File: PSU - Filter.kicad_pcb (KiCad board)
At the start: 2 copper layers, 111.8 x 63.5 mm, 36 parts, among them J2 +12V, J3 GND, J4 -12V, J5 +12 GND -12, U1 LM317, U2 LM337

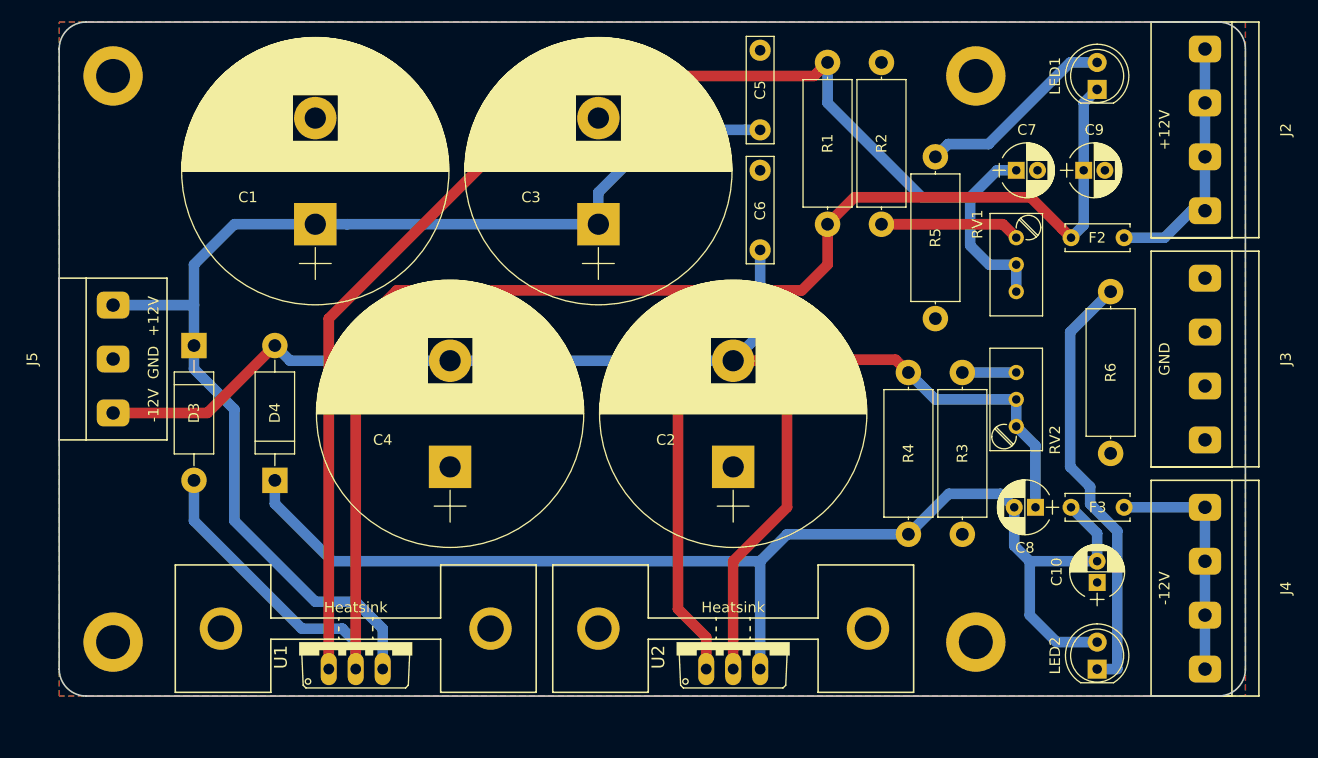
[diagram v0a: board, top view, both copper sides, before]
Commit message: Release client. Fixed a short in +12 branch Changed 10uF footprint to 6.3/2.5mm New KiCad standard library Pointers to the KraakenStuffLib library
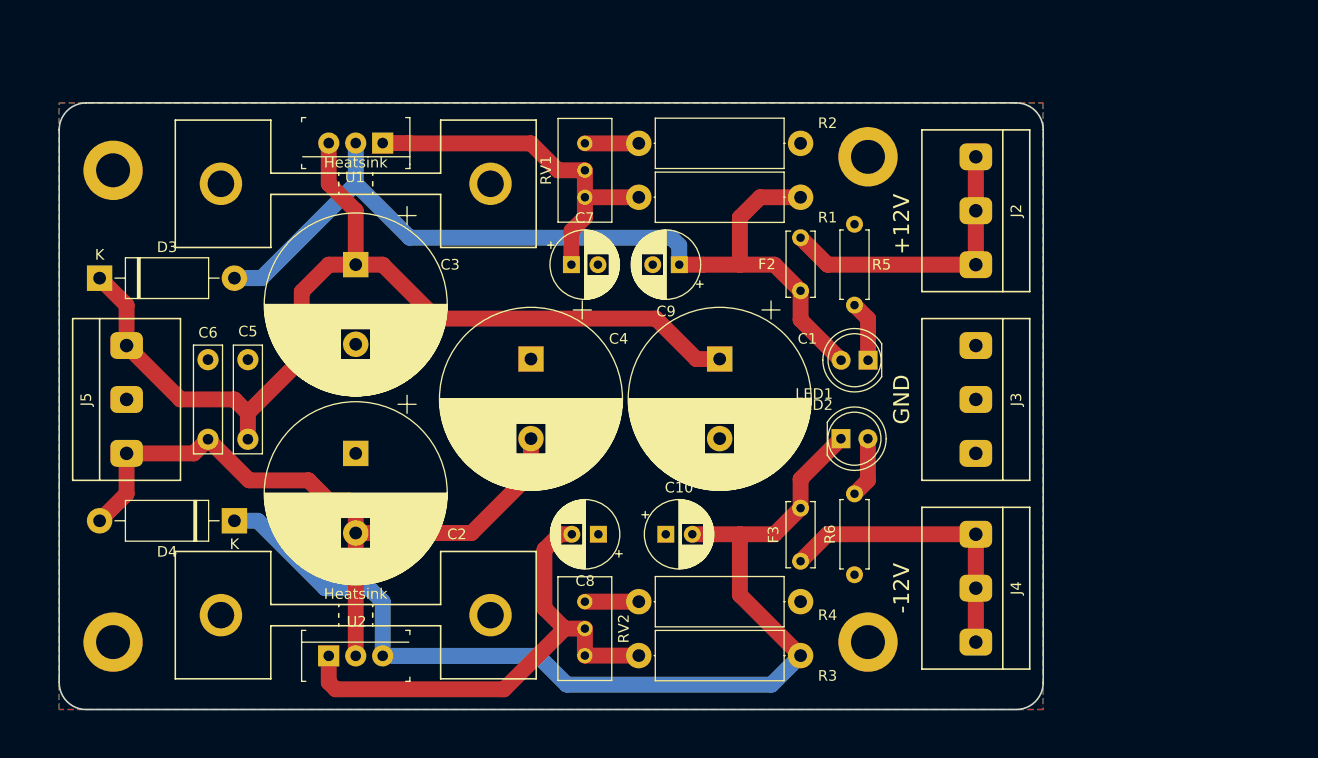
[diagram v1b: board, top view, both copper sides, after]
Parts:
- C1, C2, C3, C4: footprint Capacitors_THT:CP_Radial_D25.0mm_P10.00mm_SnapIn -> Capacitor_THT:CP_Radial_D17.0mm_P7.50mm
- C10, C7, C9: footprint Capacitors_THT:CP_Radial_D5.0mm_P2.00mm -> Capacitor_THT:CP_Radial_D6.3mm_P2.50mm
- C5, C6: footprint Capacitors_THT:C_Rect_L10.0mm_W2.5mm_P7.50mm_MKS4 -> Capacitor_THT:C_Rect_L10.0mm_W2.5mm_P7.50mm_MKS4
- C8: value 4.7u -> 10u; footprint Capacitors_THT:CP_Radial_D5.0mm_P2.00mm -> Capacitor_THT:CP_Radial_D6.3mm_P2.50mm
- D3, D4: footprint Diodes_THT:D_DO-15_P12.70mm_Horizontal -> Diode_THT:D_DO-15_P12.70mm_Horizontal
- F2, F3: footprint Capacitors_THT:C_Disc_D6.0mm_W2.5mm_P5.00mm -> Capacitor_THT:C_Disc_D6.0mm_W2.5mm_P5.00mm
- J2, J3, J4: footprint MojaBiblioteka:Klema x4 -> KraakenStuff:Klema x3
- J5: value +12 GND -12 -> PWR_IN; footprint MojaBiblioteka:Klema x3 -> KraakenStuff:Klema x3
- LED1, LED2: footprint LEDs:LED_D5.0mm -> LED_THT:LED_D5.0mm
- R1, R2, R3, R4: footprint Resistors_THT:R_Axial_DIN0414_L11.9mm_D4.5mm_P15.24mm_Horizontal -> Resistor_THT:R_Axial_DIN0414_L11.9mm_D4.5mm_P15.24mm_Horizontal
- R5, R6: footprint Resistors_THT:R_Axial_DIN0414_L11.9mm_D4.5mm_P15.24mm_Horizontal -> Resistor_THT:R_Axial_DIN0207_L6.3mm_D2.5mm_P7.62mm_Horizontal
- RV1, RV2: footprint Potentiometers:Potentiometer_Trimmer_Bourns_3296W -> Potentiometer_THT:Potentiometer_Bourns_3296W_Vertical
- U1, U2: footprint MusicThingModular:TO220V -> KraakenStuff:TO-220-3
- moved C5 56.4 mm to (81.3, 90.1)
- moved C6 55.0 mm to (77.5, 82.6)
- moved Heatsink 55.0 mm to (91.4, 66.0)
- moved U1 47.1 mm to (94.0, 62.2), turned to 180 degrees
- moved RV2 46.0 mm to (113.0, 110.5)
- moved C7 42.8 mm to (111.8, 73.7)
- moved RV1 41.6 mm to (113.0, 62.2)
- moved C8 41.3 mm to (114.3, 99.1)
- moved C10 40.9 mm to (120.7, 99.1), turned to 0 degrees
- moved C1 40.2 mm to (125.7, 82.5), turned to 270 degrees
- moved C9 39.1 mm to (121.9, 73.7), turned to 180 degrees
- moved U2 38.1 mm to (88.9, 110.5)
- moved R4 36.8 mm to (118.1, 110.5), turned to 0 degrees
- moved C2 35.6 mm to (91.4, 91.4), turned to 270 degrees
- moved LED1 33.4 mm to (139.7, 82.7), turned to 180 degrees
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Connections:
- C8 pad 1: Net-(C8-Pad1) -> GND
- C8 pad 2: Net-(C10-Pad2) -> Net-(C8-Pad2)
- LED1 pad 1: Net-(C9-Pad1) -> Net-(LED1-Pad1)
- LED1 pad 2: Net-(LED1-Pad2) -> Net-(C9-Pad1)
- LED2 pad 1: Net-(LED2-Pad1) -> Net-(C10-Pad2)
- LED2 pad 2: Net-(C10-Pad2) -> Net-(LED2-Pad2)
- R4 pad 1: Net-(C8-Pad1) -> Net-(C8-Pad2)
- R5 pad 1: Net-(LED1-Pad2) -> Net-(LED1-Pad1)
- R6 pad 2: Net-(LED2-Pad1) -> Net-(LED2-Pad2)
- RV2 pad 1: Net-(C8-Pad1) -> Net-(C8-Pad2)
- RV2 pad 2: Net-(C8-Pad1) -> Net-(C8-Pad2)
- U2 pad 1: Net-(C8-Pad1) -> Net-(C8-Pad2)
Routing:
- net Net-(C7-Pad1): track 128.5 -> 34.6 mm
- net Net-(C8-Pad1): track 79.4 -> 0.00 mm
- net Net-(C9-Pad1): track 149.6 -> 85.2 mm
- net Net-(C8-Pad2): track 0.00 -> 48.3 mm
- net Net-(LED2-Pad1): track 40.9 -> 0.00 mm
- net -12_IN: track 108.1 -> 68.3 mm, vias 1 -> 0
- net +12_IN: track 115.7 -> 94.1 mm
- net Net-(C10-Pad2): track 118.0 -> 97.0 mm
- net Net-(LED1-Pad2): track 18.9 -> 0.00 mm
- net Net-(R2-Pad1): track 13.2 -> 5.08 mm
- net Net-(LED1-Pad1): track 0.00 -> 5.72 mm
- net Net-(LED2-Pad2): track 0.00 -> 5.72 mm
- net Net-(F3-Pad1): track 22.9 -> 27.7 mm
- net Net-(F2-Pad1): track 23.9 -> 27.7 mm
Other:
- board size 111.8 x 63.5 mm -> 92.7 x 57.2 mm
- net class Default: trace_width 1 -> 1.5
- board text removed: "-12V GND +12V"

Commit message: Finished. First round of testing passed
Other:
- board text added: "KraakenStuff PSU (filter board) v.0.2"
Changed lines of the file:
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@@
   (general
     (thickness 1.6)
-    (drawings 11)
+    (drawings 12)
     (tracks 100)
     (zones 0)
@@
       (drillshape 0)
       (scaleselection 1)
-      (outputdirectory "Gerber Filter Alternative/"))
+      (outputdirectory "Gerber/"))
   )
   (net 0 "")
@@
   (module "MojaBiblioteka:ALUMINIJUMSKI HLADNJAK TO-220_25" (layer F.Cu)
     (at 91.44 66.04)
-    (fp_text reference Heatsink (at 0 -2) (layer F.SilkS)
+    (fp_text reference Heatsink (at 0 1.8796 180) (layer F.SilkS)
       (effects (font (size 1 1) (thickness 0.15)))
     )
@@
     (descr "CP, Radial series, Radial, pin pitch=7.50mm, , diameter=17mm, Electrolytic Capacitor")
     (tags "CP Radial series Radial pin pitch 7.50mm  diameter 17mm Electrolytic Capacitor")
-    (fp_text reference C2 (at 7.62 -9.525) (layer F.SilkS)
+    (fp_text reference C2 (at 7.5946 -9.3472) (layer F.SilkS)
       (effects (font (size 1 1) (thickness 0.15)))
     )
@@
     (descr "CP, Radial series, Radial, pin pitch=7.50mm, , diameter=17mm, Electrolytic Capacitor")
     (tags "CP Radial series Radial pin pitch 7.50mm  diameter 17mm Electrolytic Capacitor")
-    (fp_text reference C3 (at 0 -8.89) (layer F.SilkS)
+    (fp_text reference C3 (at -0.0508 -9.3472) (layer F.SilkS)
       (effects (font (size 1 1) (thickness 0.15)))
     )
@@
     (descr "LED, diameter 5.0mm, 2 pins, http://cdn-reichelt.de/documents/datenblatt/A500/LL-504BC2E-009.pdf")
     (tags "LED diameter 5.0mm 2 pins")
-    (fp_text reference LED1 (at 5.08 -3.175 180) (layer F.SilkS)
+    (fp_text reference LED1 (at -2.7382 2.704133 180) (layer F.SilkS)
       (effects (font (size 1 1) (thickness 0.15)))
     )
@@
     (descr "LED, diameter 5.0mm, 2 pins, http://cdn-reichelt.de/documents/datenblatt/A500/LL-504BC2E-009.pdf")
     (tags "LED diameter 5.0mm 2 pins")
-    (fp_text reference LED2 (at -2.54 -3.175) (layer F.SilkS)
+    (fp_text reference LED2 (at 5.339 2.780334) (layer F.SilkS)
       (effects (font (size 1 1) (thickness 0.15)))
     )
@@
     (descr "Resistor, Axial_DIN0207 series, Axial, Horizontal, pin pitch=7.62mm, 0.25W = 1/4W, length*diameter=6.3*2.5mm^2, http://cdn-reichelt.de/documents/datenblatt/B400/1_4W%23YAG.pdf")
     (tags "Resistor Axial_DIN0207 series Axial Horizontal pin pitch 7.62mm 0.25W = 1/4W length 6.3mm diameter 2.5mm")
-    (fp_text reference R5 (at 3.81 2.54 180) (layer F.SilkS)
+    (fp_text reference R5 (at 3.81 2.54 270) (layer F.SilkS)
       (effects (font (size 1 1) (thickness 0.15)))
     )
@@
     (descr "Resistor, Axial_DIN0207 series, Axial, Horizontal, pin pitch=7.62mm, 0.25W = 1/4W, length*diameter=6.3*2.5mm^2, http://cdn-reichelt.de/documents/datenblatt/B400/1_4W%23YAG.pdf")
     (tags "Resistor Axial_DIN0207 series Axial Horizontal pin pitch 7.62mm 0.25W = 1/4W length 6.3mm diameter 2.5mm")
-    (fp_text reference R6 (at 3.81 -2.31 90) (layer F.SilkS)
+    (fp_text reference R6 (at 3.7592 2.54 90) (layer F.SilkS)
       (effects (font (size 1 1) (thickness 0.15)))
     )
@@
     (descr "Potentiometer, vertical, Bourns 3296W, https://www.bourns.com/pdfs/3296.pdf")
     (tags "Potentiometer vertical Bourns 3296W")
-    (fp_text reference RV2 (at -2.54 -3.66 270) (layer F.SilkS)
+    (fp_text reference RV2 (at -2.54 3.4036 270) (layer F.SilkS)
       (effects (font (size 1 1) (thickness 0.15)))
     )
@@
     (at 93.98 62.2046 180)
     (descr http://www.st.com/content/ccc/resource/technical/document/datasheet/f9/ed/f5/44/26/b9/43/a4/CD00000911.pdf/files/CD00000911.pdf/jcr:content/translations/en.CD00000911.pdf)
-    (fp_text reference U1 (at 2.62 -3.22 180) (layer F.SilkS)
+    (fp_text reference U1 (at 9.1694 -0.0254 180) (layer F.SilkS)
       (effects (font (size 1 1) (thickness 0.15)))
     )
@@
     (at 88.9 110.5154)
     (descr http://www.st.com/content/ccc/resource/technical/document/datasheet/f9/ed/f5/44/26/b9/43/a4/CD00000911.pdf/files/CD00000911.pdf/jcr:content/translations/en.CD00000911.pdf)
-    (fp_text reference U2 (at 2.62 -3.22) (layer F.SilkS)
+    (fp_text reference U2 (at -4.0894 0) (layer F.SilkS)
       (effects (font (size 1 1) (thickness 0.15)))
     )
@@
     (descr "Diode, DO-15 series, Axial, Horizontal, pin pitch=12.7mm, , length*diameter=7.6*3.6mm^2, , http://www.diodes.com/_files/packages/DO-15.pdf")
     (tags "Diode DO-15 series Axial Horizontal pin pitch 12.7mm  length 7.6mm diameter 3.6mm")
-    (fp_text reference D3 (at 6.35 -2.92) (layer F.SilkS)
+    (fp_text reference D3 (at 3.2258 -3.2766) (layer F.SilkS)
       (effects (font (size 1 1) (thickness 0.15)))
     )
@@
       (effects (font (size 1 1) (thickness 0.15)))
     )
-    (fp_text user K (at 0 -2.2) (layer F.SilkS)
+    (fp_text user K (at 2.8448 2.8448) (layer F.SilkS)
       (effects (font (size 1 1) (thickness 0.15)))
     )
@@
     (descr "Diode, DO-15 series, Axial, Horizontal, pin pitch=12.7mm, , length*diameter=7.6*3.6mm^2, , http://www.diodes.com/_files/packages/DO-15.pdf")
     (tags "Diode DO-15 series Axial Horizontal pin pitch 12.7mm  length 7.6mm diameter 3.6mm")
-    (fp_text reference D4 (at 6.35 -2.92 180) (layer F.SilkS)
+    (fp_text reference D4 (at 9.525 -3.3274 180) (layer F.SilkS)
       (effects (font (size 1 1) (thickness 0.15)))
     )
@@
       (effects (font (size 1 1) (thickness 0.15)))
     )
-    (fp_text user K (at 0 -2.2 180) (layer F.SilkS)
+    (fp_text user K (at 2.7432 2.9464 180) (layer F.SilkS)
       (effects (font (size 1 1) (thickness 0.15)))
     )
@@
     (descr "CP, Radial series, Radial, pin pitch=2.50mm, , diameter=6.3mm, Electrolytic Capacitor")
     (tags "CP Radial series Radial pin pitch 2.50mm  diameter 6.3mm Electrolytic Capacitor")
-    (fp_text reference C7 (at 1.25 -4.4) (layer F.SilkS)
+    (fp_text reference C7 (at -3.429 -0.0508) (layer F.SilkS)
       (effects (font (size 1 1) (thickness 0.15)))
     )
@@
     (descr "CP, Radial series, Radial, pin pitch=2.50mm, , diameter=6.3mm, Electrolytic Capacitor")
     (tags "CP Radial series Radial pin pitch 2.50mm  diameter 6.3mm Electrolytic Capacitor")
-    (fp_text reference C8 (at 1.25 -4.4 180) (layer F.SilkS)
+    (fp_text reference C8 (at 5.969 0.0254 180) (layer F.SilkS)
       (effects (font (size 1 1) (thickness 0.15)))
     )
@@
       (effects (font (size 1 1) (thickness 0.15)))
     )
-    (fp_text user %R (at 1.25 0 180) (layer F.Fab)
+    (fp_text user %R (at 1.0414 0.0762 180) (layer F.Fab)
       (effects (font (size 1 1) (thickness 0.15)))
     )
@@
     (descr "CP, Radial series, Radial, pin pitch=2.50mm, , diameter=6.3mm, Electrolytic Capacitor")
     (tags "CP Radial series Radial pin pitch 2.50mm  diameter 6.3mm Electrolytic Capacitor")
-    (fp_text reference C9 (at 1.25 -4.4 180) (layer F.SilkS)
+    (fp_text reference C9 (at -3.3274 0.0508 180) (layer F.SilkS)
       (effects (font (size 1 1) (thickness 0.15)))
     )
@@
     (descr "CP, Radial series, Radial, pin pitch=2.50mm, , diameter=6.3mm, Electrolytic Capacitor")
     (tags "CP Radial series Radial pin pitch 2.50mm  diameter 6.3mm Electrolytic Capacitor")
-    (fp_text reference C10 (at 1.25 -4.4) (layer F.SilkS)
+    (fp_text reference C10 (at 6.2738 -0.0254) (layer F.SilkS)
       (effects (font (size 1 1) (thickness 0.15)))
     )
@@
     )
   )
+  (gr_text "KraakenStuff\nPSU (filter board) v.0.2" (at 144.653 86.360001 90) (layer B.SilkS)
+    (effects (font (size 1.5 1.5) (thickness 0.3)) (justify mirror))
+  )
   (gr_text -12V (at 142.875 104.14 90) (layer F.SilkS)

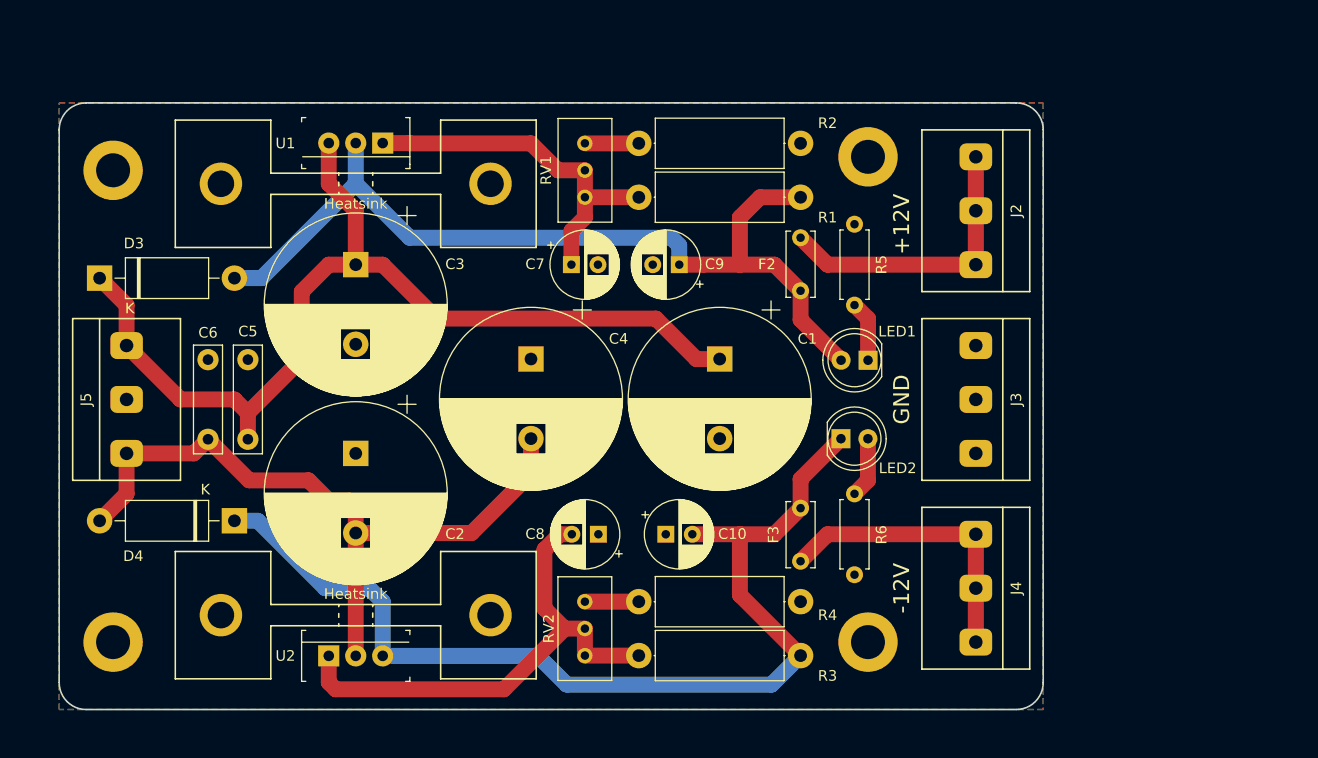
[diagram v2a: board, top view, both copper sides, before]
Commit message: Made more space between caps and heatsinks on the filter board
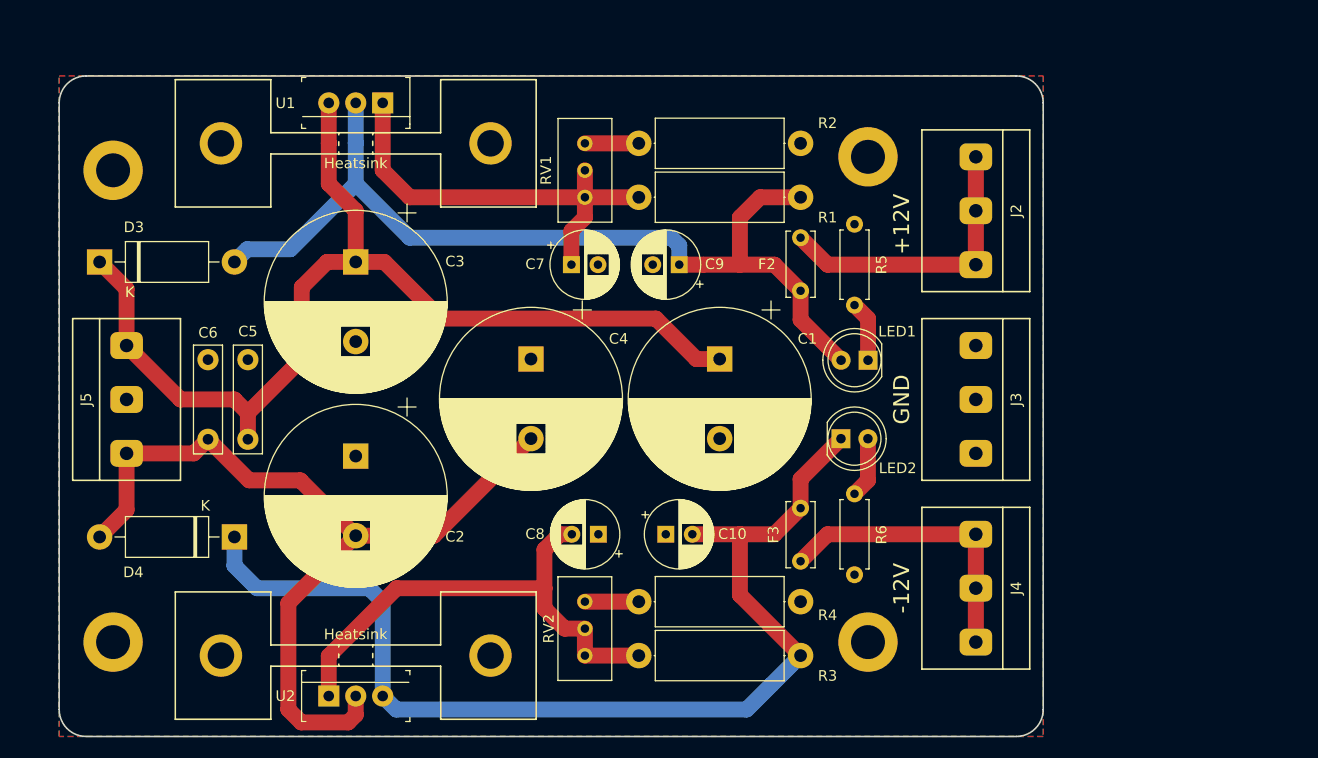
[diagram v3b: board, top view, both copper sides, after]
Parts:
- moved Heatsink 3.81 mm to (91.4, 62.2)
- moved Heatsink 3.81 mm to (91.4, 110.5)
- moved U1 3.78 mm to (94.0, 58.4)
- moved U2 3.78 mm to (88.9, 114.3)
- moved D3 1.52 mm to (67.3, 73.4)
- moved D4 1.52 mm to (80.0, 99.3)
- moved C2 0.25 mm to (91.4, 91.7)
- moved C3 0.25 mm to (91.4, 73.4)
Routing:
- net -12_IN: track 68.3 -> 83.1 mm
- net Net-(C7-Pad1): track 34.6 -> 40.9 mm
- net +12_IN: track 94.1 -> 99.7 mm
- net Net-(C10-Pad2): track 97.0 -> 102.1 mm
- net Net-(C9-Pad1): track 85.2 -> 88.3 mm
- net Net-(C8-Pad2): track 48.3 -> 47.7 mm
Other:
- board size 92.7 x 57.2 mm -> 92.7 x 62.2 mm
- board text added: "KraakenStuff PSU (filter board) v.0.3"
- board text removed: "KraakenStuff PSU (filter board) v.0.2"

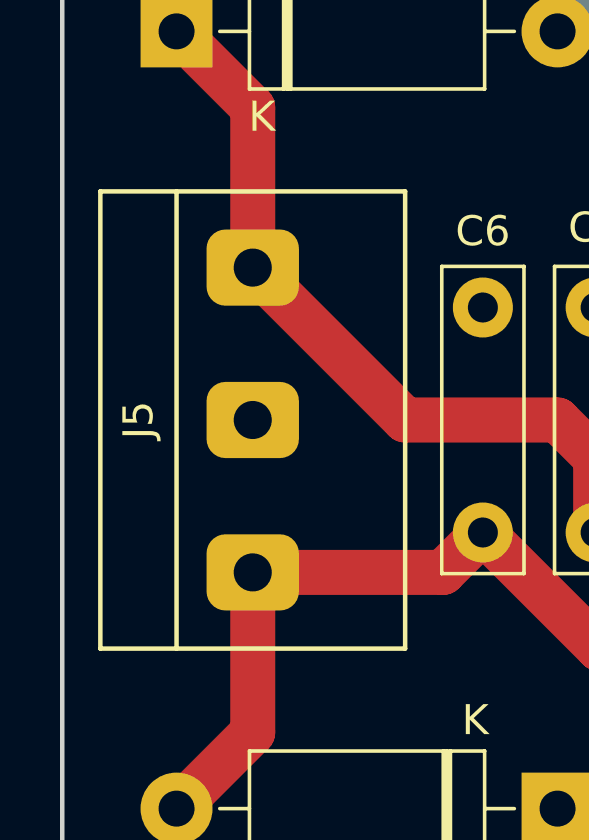
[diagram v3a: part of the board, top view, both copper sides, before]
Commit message: Added a label to the input of filter board
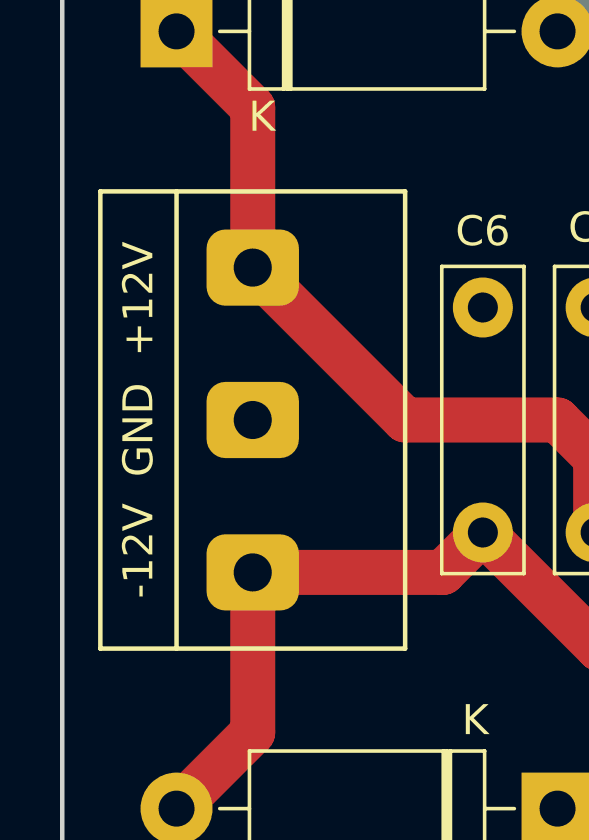
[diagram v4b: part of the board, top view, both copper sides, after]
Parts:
- -12V  GND  +12V: renamed from J5
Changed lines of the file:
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@@
   (module "KraakenStuff:Klema x3" (layer F.Cu)
     (at 69.85 86.36 270)
-    (fp_text reference J5 (at 0 3.81 270) (layer F.SilkS)
+    (fp_text reference "-12V  GND  +12V" (at 0 3.81 270) (layer F.SilkS)
       (effects (font (size 1 1) (thickness 0.15)))
     )
